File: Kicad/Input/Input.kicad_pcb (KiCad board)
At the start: 2 copper layers, 60 x 60 mm, 37 parts, among them J1 Conn_01x02, J2 Conn_01x02, J3 Conn_01x03, U1 AD8567ARUZ, U2 MAX4016ESA+, U3 LM319

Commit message: PCB for input and added filter caps
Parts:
- moved R12 1.52 mm to (166.9, -395.5)
- moved CF3 1.07 mm to (168.1, -400.1)
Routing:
- net VCC: track 81.1 -> 77.9 mm
- net /Comparator/PWM_OUT: track 23.3 -> 24.9 mm
- net GND: vias 16 -> 19

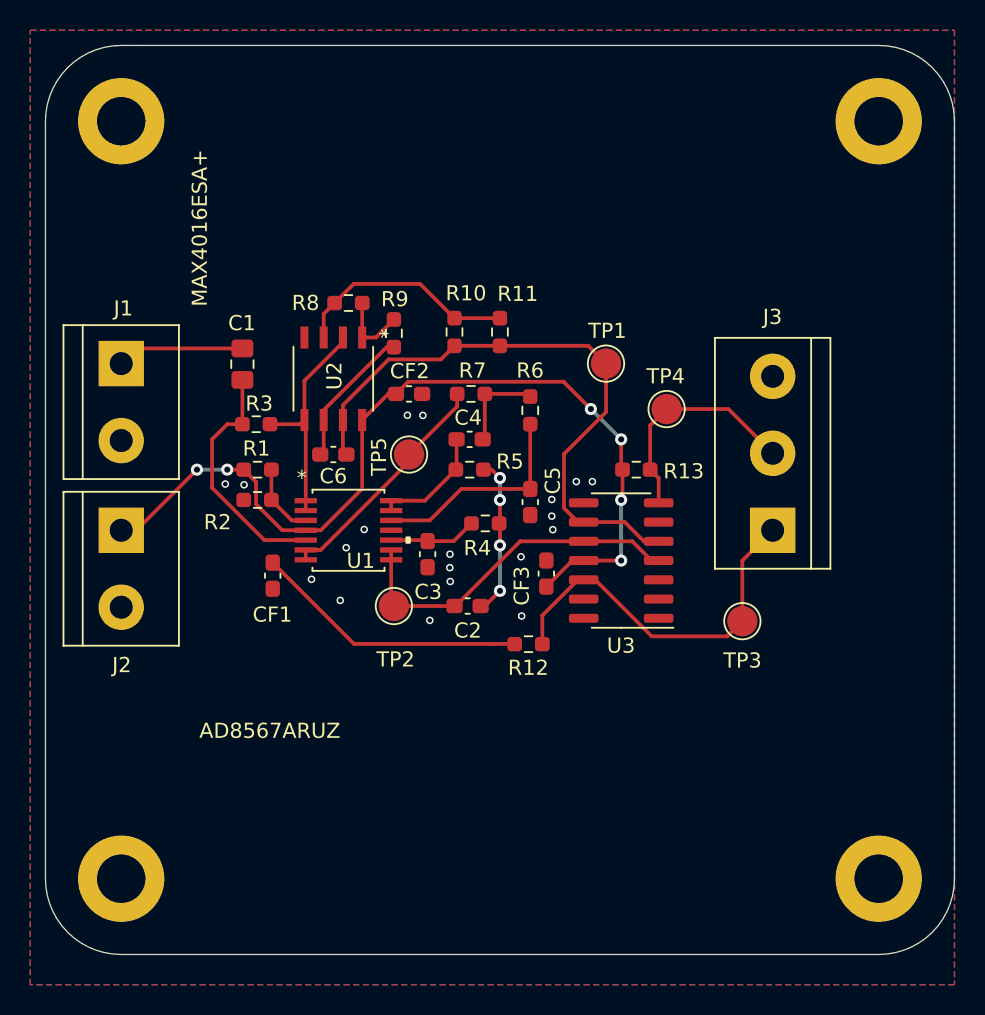
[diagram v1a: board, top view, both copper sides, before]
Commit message: resized input board
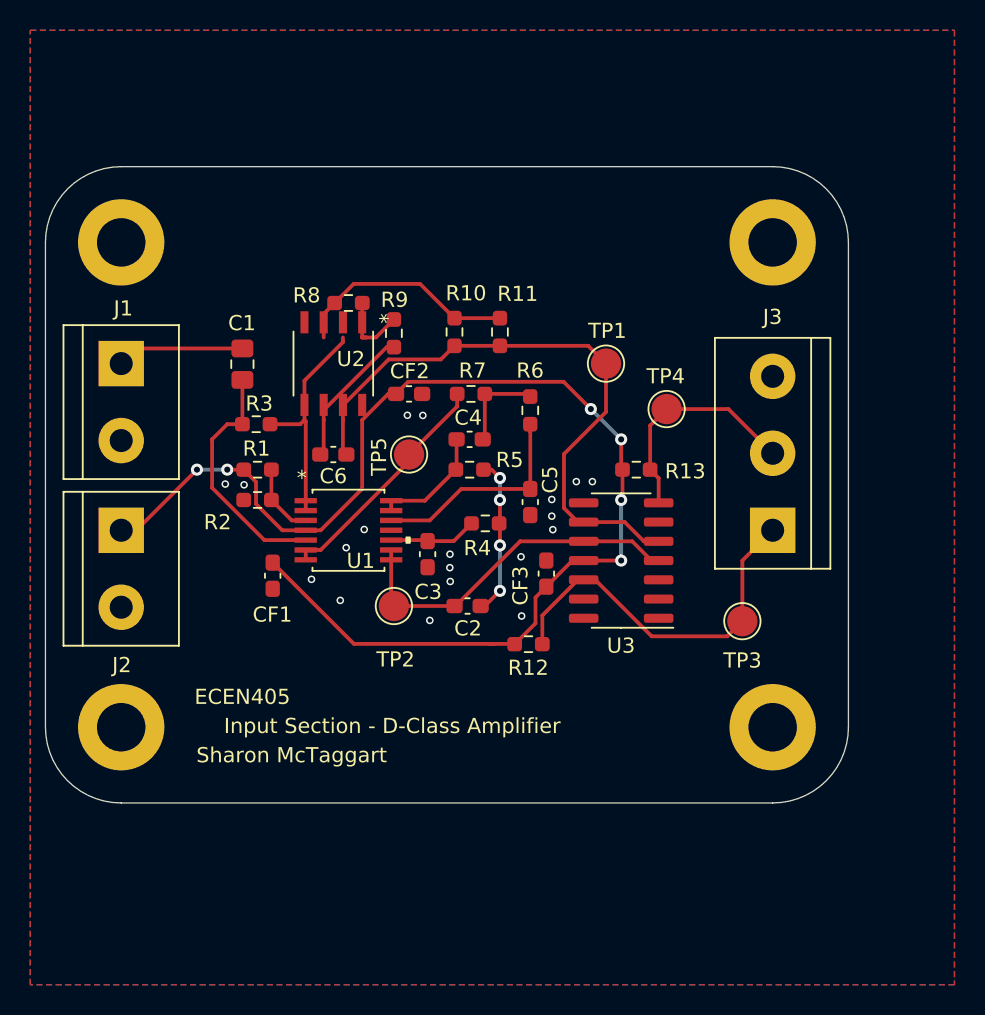
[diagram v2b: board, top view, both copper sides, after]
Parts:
- moved H4 12.2 mm to (183.0, -390.0)
- moved H2 10.6 mm to (183.0, -422.0)
- moved H3 10.0 mm to (140.0, -390.0)
- moved H1 8.00 mm to (140.0, -422.0)
- moved U2 1.00 mm to (154.0, -414.0)
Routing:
- net VCC: track 77.9 -> 82.5 mm
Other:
- board size 60 x 60 mm -> 53 x 42 mm
- board text added: "ECEN405"
- board text added: "Input Section - D-Class Amplifier"
- board text added: "Sharon McTaggart"

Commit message: added gerber and drill files
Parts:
- moved R8 0.88 mm to (154.8, -418.9)
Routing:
- net /LPF/VREF: track 14.9 -> 16.0 mm
- net VCC: track 82.5 -> 83.5 mm
- net Net-(R8-Pad1): track 5.15 -> 6.09 mm
- net Net-(C6-Pad2): track 9.38 -> 10.3 mm
- net /Comparator/TRIANGLE_IN: track 40.7 -> 41.5 mm
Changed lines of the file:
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@@
     (thickness 1.6)
     (drawings 12)
-    (tracks 181)
+    (tracks 190)
     (zones 0)
     (modules 37)
@@
     (pcbplotparams
       (layerselection 0x010fc_ffffffff)
-      (usegerberextensions false)
-      (usegerberattributes true)
-      (usegerberadvancedattributes true)
-      (creategerberjobfile true)
+      (usegerberextensions true)
+      (usegerberattributes false)
+      (usegerberadvancedattributes false)
+      (creategerberjobfile false)
       (excludeedgelayer true)
       (linewidth 0.100000)
@@
       (psa4output false)
       (plotreference true)
-      (plotvalue true)
+      (plotvalue false)
       (plotinvisibletext false)
       (padsonsilk false)
-      (subtractmaskfromsilk false)
+      (subtractmaskfromsilk true)
       (outputformat 1)
       (mirror false)
-      (drillshape 1)
+      (drillshape 0)
       (scaleselection 1)
-      (outputdirectory ""))
+      (outputdirectory "input_gerbers"))
   )
   (net 0 "")
@@
       (effects (font (size 1 1) (thickness 0.15)))
     )
-    (fp_text user "Copyright 2021 Accelerated Designs. All rights reserved." (at 0 0 90) (layer Cmts.User)
+    (fp_text user "Copyright 2021 Accelerated Designs. All rights reserved." (at 0 0 90) (layer Cmts.User) hide
       (effects (font (size 0.127 0.127) (thickness 0.002)))
     )
@@
       (effects (font (size 1 1) (thickness 0.15)))
     )
-    (fp_text user "Copyright 2021 Accelerated Designs. All rights reserved." (at 0 0) (layer Cmts.User)
+    (fp_text user "Copyright 2021 Accelerated Designs. All rights reserved." (at 0 0) (layer Cmts.User) hide
       (effects (font (size 0.127 0.127) (thickness 0.002)))
     )
@@
   )
   (module Resistor_SMD:R_0603_1608Metric_Pad0.98x0.95mm_HandSolder (layer F.Cu)
-    (at 155 -418 180)
+    (at 154.7675 -418.85 180)
     (descr "Resistor SMD 0603 (1608 Metric), square (rectangular) end terminal, IPC_7351 nominal with elongated pad for handsoldering. (Body size source: IPC-SM-782 page 72, https://www.pcb-3d.com/wordpress/wp-content/uploads/ipc-sm-782a_amendment_1_and_2.pdf), generated with kicad-footprint-generator")
     (tags "resistor handsolder")
     (attr smd)
-    (fp_text reference R8 (at 2.76 0.5) (layer F.SilkS)
+    (fp_text reference R8 (at 2.7775 -0.13) (layer F.SilkS)
       (effects (font (size 1 1) (thickness 0.15)))
     )
@@
       (effects (font (size 0.5 0.5) (thickness 0.08)))
     )
-    (pad 2 smd roundrect (at 1.0375 0 90) (size 1.175 1.45) (layers F.Cu F.Paste F.Mask) (roundrect_rratio 0.212766)
+    (pad 2 smd roundrect (at 1.0375 0 90) (size 1.175 1.45) (layers F.Cu F.Paste F.Mask) (roundrect_rratio 0.2127659574468085)
       (net 1 /LPF/SIG_IN))
-    (pad 1 smd roundrect (at -1.0375 0 90) (size 1.175 1.45) (layers F.Cu F.Paste F.Mask) (roundrect_rratio 0.212766)
+    (pad 1 smd roundrect (at -1.0375 0 90) (size 1.175 1.45) (layers F.Cu F.Paste F.Mask) (roundrect_rratio 0.2127659574468085)
       (net 2 "Net-(C1-Pad1)"))
     (model ${KISYS3DMOD}/Capacitor_SMD.3dshapes/C_0805_2012Metric.wrl
@@
   (segment (start 153.365 -410.27585) (end 153.365 -408.2275) (width 0.25) (layer F.Cu) (net 10))
   (segment (start 153.365 -410.9275) (end 153.365 -410.27585) (width 0.25) (layer F.Cu) (net 10))
-  (segment (start 157.525 -415.0875) (end 153.365 -410.9275) (width 0.25) (layer F.Cu) (net 10))
   (segment (start 158 -415.0875) (end 157.525 -415.0875) (width 0.25) (layer F.Cu) (net 10))
+  (segment (start 156.1964 -415.0875) (end 158 -415.0875) (width 0.25) (layer F.Cu) (net 10))
+  (segment (start 153.365 -412.2561) (end 156.1964 -415.0875) (width 0.25) (layer F.Cu) (net 10))
+  (segment (start 153.365 -411.27585) (end 153.365 -412.2561) (width 0.25) (layer F.Cu) (net 10))
   (segment (start 154.635 -408.2275) (end 154.8625 -408) (width 0.25) (layer F.Cu) (net 11))
   (segment (start 154.635 -410.27585) (end 154.635 -408.2275) (width 0.25) (layer F.Cu) (net 11))
@@
   (segment (start 175.475 -402.27) (end 174.5 -402.27) (width 0.25) (layer F.Cu) (net 11))
   (segment (start 161.09999 -414.27499) (end 162 -415.175) (width 0.25) (layer F.Cu) (net 11))
-  (segment (start 157.65389 -414.27499) (end 161.09999 -414.27499) (width 0.25) (layer F.Cu) (net 11))
-  (segment (start 154.635 -411.2561) (end 157.65389 -414.27499) (width 0.25) (layer F.Cu) (net 11))
   (segment (start 154.635 -410.27585) (end 154.635 -411.2561) (width 0.25) (layer F.Cu) (net 11))
   (segment (start 170.148232 -403.54) (end 170.525 -403.54) (width 0.25) (layer F.Cu) (net 11))
@@
   (segment (start 172 -410.80449) (end 169.22499 -408.02948) (width 0.25) (layer F.Cu) (net 11))
   (segment (start 172 -414) (end 172 -410.80449) (width 0.25) (layer F.Cu) (net 11))
+  (segment (start 156.65389 -414.27499) (end 157.90499 -414.27499) (width 0.25) (layer F.Cu) (net 11))
+  (segment (start 154.635 -412.2561) (end 156.65389 -414.27499) (width 0.25) (layer F.Cu) (net 11))
+  (segment (start 154.635 -411.27585) (end 154.635 -412.2561) (width 0.25) (layer F.Cu) (net 11))
+  (segment (start 157.90499 -414.27499) (end 161.09999 -414.27499) (width 0.25) (layer F.Cu) (net 11))
+  (segment (start 157.65389 -414.27499) (end 157.90499 -414.27499) (width 0.25) (layer F.Cu) (net 11))
   (segment (start 157.62915 -412) (end 155.905 -410.27585) (width 0.25) (layer F.Cu) (net 12))
   (segment (start 158.1375 -412) (end 157.62915 -412) (width 0.25) (layer F.Cu) (net 12))
@@
   (segment (start 167.34499 -398.56249) (end 167.34499 -396.85499) (width 0.25) (layer F.Cu) (net 12))
   (segment (start 168.06 -399.2775) (end 167.34499 -398.56249) (width 0.25) (layer F.Cu) (net 12))
+  (segment (start 155.905 -410.27585) (end 155.905 -411.27585) (width 0.25) (layer F.Cu) (net 12))
   (segment (start 175.475 -406.4375) (end 174.9125 -407) (width 0.25) (layer F.Cu) (net 13))
   (segment (start 175.475 -404.81) (end 175.475 -406.4375) (width 0.25) (layer F.Cu) (net 13))
@@
   (segment (start 152.1806 -410.19025) (end 152.095 -410.27585) (width 0.25) (layer F.Cu) (net 16))
   (segment (start 152.1806 -404.950001) (end 152.1806 -410.19025) (width 0.25) (layer F.Cu) (net 16))
-  (segment (start 154.635 -415.412198) (end 154.635 -415.72415) (width 0.25) (layer F.Cu) (net 16))
-  (segment (start 152.095 -412.872198) (end 154.635 -415.412198) (width 0.25) (layer F.Cu) (net 16))
-  (segment (start 152.095 -410.27585) (end 152.095 -412.872198) (width 0.25) (layer F.Cu) (net 16))
+  (segment (start 152.1806 -411.19025) (end 152.095 -411.27585) (width 0.25) (layer F.Cu) (net 16))
+  (segment (start 152.1806 -410.19025) (end 152.1806 -411.19025) (width 0.25) (layer F.Cu) (net 16))
+  (segment (start 154.635 -416.412198) (end 154.635 -416.72415) (width 0.25) (layer F.Cu) (net 16))
+  (segment (start 152.095 -413.872198) (end 154.635 -416.412198) (width 0.25) (layer F.Cu) (net 16))
+  (segment (start 152.095 -411.27585) (end 152.095 -413.872198) (width 0.25) (layer F.Cu) (net 16))
   (segment (start 152.1806 -401.7) (end 152.1806 -401.050001) (width 0.25) (layer F.Cu) (net 17))
   (segment (start 153.1672 -401.7) (end 159 -407.5328) (width 0.25) (layer F.Cu) (net 17))
@@
   (segment (start 162.175 -411.175) (end 162.175 -412) (width 0.25) (layer F.Cu) (net 17))
   (segment (start 159 -408) (end 162.175 -411.175) (width 0.25) (layer F.Cu) (net 17))
-  (segment (start 153.365 -417.2775) (end 154.0875 -418) (width 0.25) (layer F.Cu) (net 18))
-  (segment (start 153.365 -415.72415) (end 153.365 -417.2775) (width 0.25) (layer F.Cu) (net 18))
   (segment (start 162 -417) (end 165 -417) (width 0.25) (layer F.Cu) (net 18))
   (segment (start 162 -417) (end 162 -417.01) (width 0.25) (layer F.Cu) (net 18))
   (segment (start 162 -417) (end 161.99 -417) (width 0.25) (layer F.Cu) (net 18))
-  (segment (start 161.99 -417) (end 159.73 -419.26) (width 0.25) (layer F.Cu) (net 18))
-  (segment (start 155.3475 -419.26) (end 154.0875 -418) (width 0.25) (layer F.Cu) (net 18))
-  (segment (start 159.73 -419.26) (end 155.3475 -419.26) (width 0.25) (layer F.Cu) (net 18))
-  (segment (start 155.905 -417.9925) (end 155.9125 -418) (width 0.25) (layer F.Cu) (net 19))
-  (segment (start 155.905 -415.72415) (end 155.905 -417.9925) (width 0.25) (layer F.Cu) (net 19))
+  (segment (start 153.365 -418.36) (end 153.855 -418.85) (width 0.25) (layer F.Cu) (net 18))
+  (segment (start 153.365 -416.72415) (end 153.365 -418.36) (width 0.25) (layer F.Cu) (net 18))
+  (segment (start 153.855 -418.85) (end 153.855 -418.855) (width 0.25) (layer F.Cu) (net 18))
+  (segment (start 159.34999 -419.65001) (end 162 -417) (width 0.25) (layer F.Cu) (net 18))
+  (segment (start 154.65001 -419.65001) (end 159.34999 -419.65001) (width 0.25) (layer F.Cu) (net 18))
+  (segment (start 153.855 -418.855) (end 154.65001 -419.65001) (width 0.25) (layer F.Cu) (net 18))
   (segment (start 155.905 -415.72415) (end 156.18835 -415.72415) (width 0.25) (layer F.Cu) (net 19))
   (segment (start 156.81165 -415.72415) (end 158 -416.9125) (width 0.25) (layer F.Cu) (net 19))
   (segment (start 155.905 -415.72415) (end 156.81165 -415.72415) (width 0.25) (layer F.Cu) (net 19))
+  (segment (start 155.905 -418.625) (end 155.68 -418.85) (width 0.25) (layer F.Cu) (net 19))
+  (segment (start 155.905 -415.72415) (end 155.905 -418.625) (width 0.25) (layer F.Cu) (net 19))
   (zone (net 5) (net_name GND) (layer B.Cu) (hatch edge 0.508)
     (connect_pads (clearance 0.508))
